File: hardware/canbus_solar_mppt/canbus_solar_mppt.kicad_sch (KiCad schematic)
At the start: 19 parts

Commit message: WIP: complete DC/DC engine
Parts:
- added F? (x2): MC011014, Fuse:Fuse_2920_7451Metric_Pad2.10x5.45mm_HandSolder, symbol Device:Polyfuse_Small
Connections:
- net DC-DC/SOLAR_PWR: now also F?.1; no longer D?.2 (A)
- net logic_canbus/CAN_PWR: now also F?.1; no longer D?.2 (A)
- new net: D?.2 (A), F?.2 (x2)
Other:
- moved on the sheet: D?

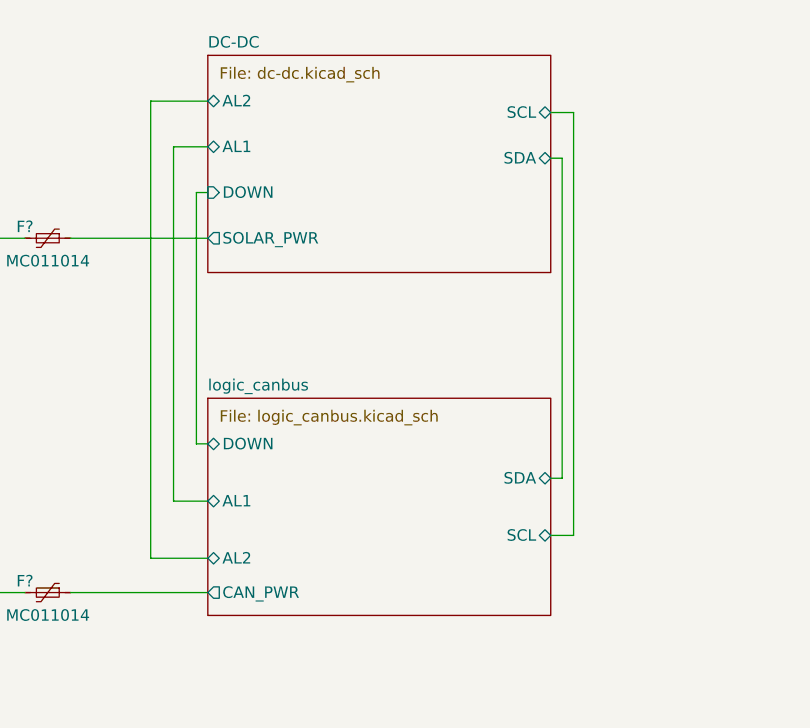
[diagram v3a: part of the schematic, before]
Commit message: Add more signals between pic18 and DC/DC
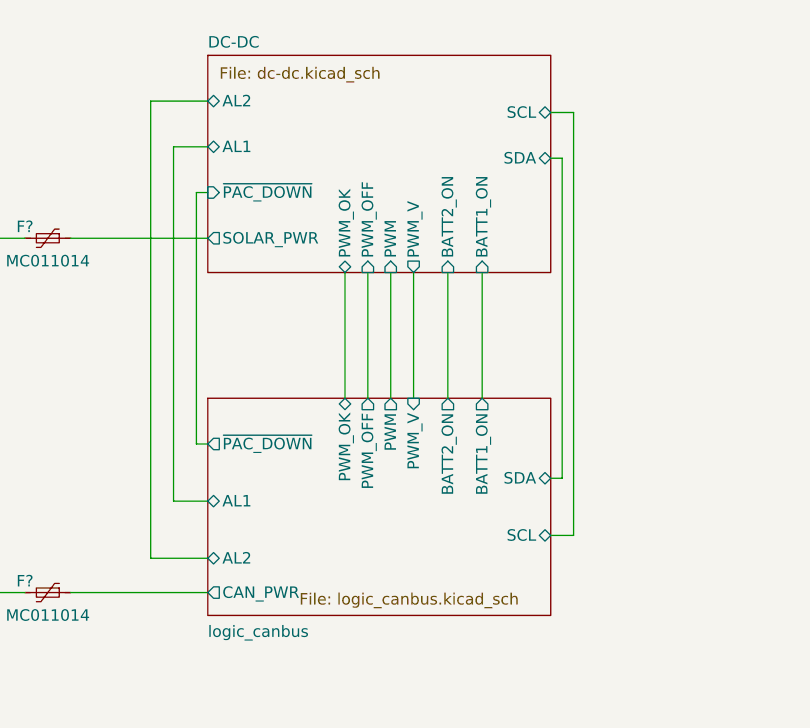
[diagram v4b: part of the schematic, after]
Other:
- sheet DC-DC ports: added BATT1_ON, BATT2_ON, PWM, PWM_OFF, PWM_OK, PWM_V, ~{PAC_DOWN}; removed DOWN
- sheet logic_canbus ports: added BATT1_ON, BATT2_ON, PWM, PWM_OFF, PWM_OK, PWM_V, ~{PAC_DOWN}; removed DOWN
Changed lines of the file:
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@@
+    (stroke (width 0) (type default) (color 0 0 0 0))
+  )
+  (wire (pts (xy 201.93 59.69) (xy 201.93 73.66))
     (stroke (width 0) (type default) (color 0 0 0 0))
   )
@@
     (stroke (width 0) (type default) (color 0 0 0 0))
   )
+  (wire (pts (xy 189.23 59.69) (xy 189.23 73.66))
+    (stroke (width 0) (type default) (color 0 0 0 0))
+  )
   (wire (pts (xy 63.5 93.98) (xy 53.34 93.98))
     (stroke (width 0) (type default) (color 0 0 0 0))
@@
     (stroke (width 0) (type default) (color 0 0 0 0))
   )
+  (wire (pts (xy 191.77 59.69) (xy 191.77 73.66))
+    (stroke (width 0) (type default) (color 0 0 0 0))
+  )
+  (wire (pts (xy 186.69 59.69) (xy 186.69 73.66))
+    (stroke (width 0) (type default) (color 0 0 0 0))
+  )
   (wire (pts (xy 119.38 86.36) (xy 119.38 87.63))
     (stroke (width 0) (type default) (color 0 0 0 0))
@@
     (stroke (width 0) (type default) (color 0 0 0 0))
   )
+  (wire (pts (xy 194.31 59.69) (xy 194.31 73.66))
+    (stroke (width 0) (type default) (color 0 0 0 0))
+  )
   (wire (pts (xy 165.1 40.64) (xy 165.1 91.44))
     (stroke (width 0) (type default) (color 0 0 0 0))
@@
   )
   (wire (pts (xy 53.34 67.31) (xy 57.15 67.31))
+    (stroke (width 0) (type default) (color 0 0 0 0))
+  )
+  (wire (pts (xy 198.12 59.69) (xy 198.12 73.66))
     (stroke (width 0) (type default) (color 0 0 0 0))
   )
@@
       (effects (font (size 1.27 1.27)) (justify left))
     )
-    (pin "DOWN" input (at 171.45 50.8 180)
-      (effects (font (size 1.27 1.27)) (justify left))
-    )
     (pin "SCL" bidirectional (at 209.55 41.91 0)
       (effects (font (size 1.27 1.27)) (justify right))
@@
     )
     (pin "SOLAR_PWR" output (at 171.45 55.88 180)
+      (effects (font (size 1.27 1.27)) (justify left))
+    )
+    (pin "BATT1_ON" input (at 201.93 59.69 270)
+      (effects (font (size 1.27 1.27)) (justify left))
+    )
+    (pin "PWM_V" output (at 194.31 59.69 270)
+      (effects (font (size 1.27 1.27)) (justify left))
+    )
+    (pin "BATT2_ON" input (at 198.12 59.69 270)
+      (effects (font (size 1.27 1.27)) (justify left))
+    )
+    (pin "PWM" input (at 191.77 59.69 270)
+      (effects (font (size 1.27 1.27)) (justify left))
+    )
+    (pin "PWM_OFF" input (at 189.23 59.69 270)
+      (effects (font (size 1.27 1.27)) (justify left))
+    )
+    (pin "PWM_OK" bidirectional (at 186.69 59.69 270)
+      (effects (font (size 1.27 1.27)) (justify left))
+    )
+    (pin "~{PAC_DOWN}" input (at 171.45 50.8 180)
       (effects (font (size 1.27 1.27)) (justify left))
     )
@@
     (stroke (width 0.1524) (type solid) (color 0 0 0 0))
     (fill (color 0 0 0 0.0000))
-    (property "Sheet name" "logic_canbus" (id 0) (at 171.45 72.9484 0)
+    (property "Sheet name" "logic_canbus" (id 0) (at 171.45 100.33 0)
       (effects (font (size 1.27 1.27)) (justify left bottom))
     )
-    (property "Sheet file" "logic_canbus.kicad_sch" (id 1) (at 172.72 74.93 0)
+    (property "Sheet file" "logic_canbus.kicad_sch" (id 1) (at 181.61 95.25 0)
       (effects (font (size 1.27 1.27)) (justify left top))
     )
@@
       (effects (font (size 1.27 1.27)) (justify right))
     )
-    (pin "DOWN" bidirectional (at 171.45 78.74 180)
+    (pin "~{PAC_DOWN}" output (at 171.45 78.74 180)
       (effects (font (size 1.27 1.27)) (justify left))
     )
@@
     (pin "CAN_PWR" output (at 171.45 95.25 180)
       (effects (font (size 1.27 1.27)) (justify left))
+    )
+    (pin "BATT1_ON" output (at 201.93 73.66 90)
+      (effects (font (size 1.27 1.27)) (justify right))
+    )
+    (pin "BATT2_ON" output (at 198.12 73.66 90)
+      (effects (font (size 1.27 1.27)) (justify right))
+    )
+    (pin "PWM_OFF" output (at 189.23 73.66 90)
+      (effects (font (size 1.27 1.27)) (justify right))
+    )
+    (pin "PWM_OK" bidirectional (at 186.69 73.66 90)
+      (effects (font (size 1.27 1.27)) (justify right))
+    )
+    (pin "PWM_V" input (at 194.31 73.66 90)
+      (effects (font (size 1.27 1.27)) (justify right))
+    )
+    (pin "PWM" output (at 191.77 73.66 90)
+      (effects (font (size 1.27 1.27)) (justify right))
     )
   )
@@
   )
   (symbol_instances
+    (path "/650b59c2-5f26-43cd-9e0c-72411aac3a49/02a51f57-3cf7-4e89-908d-048e0d55fd26"
+      (reference "#PWR?") (unit 1) (value "+5V") (footprint "")
+    )
     (path "/f749a8fe-5d5e-4748-ac37-3f3af8e2d0e8/046e9038-4a0e-4916-bc81-c5a27330b44e"
       (reference "#PWR?") (unit 1) (value "GND") (footprint "")
@@
       (reference "#PWR?") (unit 1) (value "GND") (footprint "")
     )
-    (path "/f749a8fe-5d5e-4748-ac37-3f3af8e2d0e8/befe8fb1-a994-45cc-8694-9d88f872ac5f"
-      (reference "#PWR?") (unit 1) (value "+5V") (footprint "")
-    )
     (path "/f749a8fe-5d5e-4748-ac37-3f3af8e2d0e8/bf27126d-2777-4e0c-8caa-229656dcb0fb"
       (reference "#PWR?") (unit 1) (value "+5V") (footprint "")
@@
     (path "/f749a8fe-5d5e-4748-ac37-3f3af8e2d0e8/c454ed80-5ad3-4205-b918-facb4559323c"
       (reference "#PWR?") (unit 1) (value "+5V") (footprint "")
-    )
-    (path "/f749a8fe-5d5e-4748-ac37-3f3af8e2d0e8/d0d5a83a-b1b9-4d26-908e-57f07485e447"
-      (reference "#PWR?") (unit 1) (value "GND") (footprint "")
     )
     (path "/650b59c2-5f26-43cd-9e0c-72411aac3a49/d743ffcd-5c13-44a3-b446-e3faf3dce348"
@@
       (reference "R?") (unit 1) (value "10K") (footprint "Resistor_THT:R_Axial_DIN0207_L6.3mm_D2.5mm_P7.62mm_Horizontal")
     )
-    (path "/f749a8fe-5d5e-4748-ac37-3f3af8e2d0e8/69c9f6b8-5c4a-495f-afae-470fc09b9bd9"
-      (reference "R?") (unit 1) (value "10K") (footprint "Resistor_SMD:R_1206_3216Metric_Pad1.30x1.75mm_HandSolder")
+    (path "/f749a8fe-5d5e-4748-ac37-3f3af8e2d0e8/723c4808-e36f-43cc-acdc-220d7731d5d3"
+      (reference "R?") (unit 1) (value "10K") (footprint "Resistor_THT:R_Axial_DIN0207_L6.3mm_D2.5mm_P7.62mm_Horizontal")
     )
     (path "/650b59c2-5f26-43cd-9e0c-72411aac3a49/758adae9-6fdc-4790-99a7-0cd4055f8e5d"
@@
       (reference "R?") (unit 1) (value "10K") (footprint "Resistor_SMD:R_1206_3216Metric_Pad1.30x1.75mm_HandSolder")
     )
+    (path "/650b59c2-5f26-43cd-9e0c-72411aac3a49/9d57c1ba-3976-407f-8594-55ec91182989"
+      (reference "R?") (unit 1) (value "56K") (footprint "Resistor_THT:R_Axial_DIN0207_L6.3mm_D2.5mm_P7.62mm_Horizontal")
+    )
+    (path "/f749a8fe-5d5e-4748-ac37-3f3af8e2d0e8/9e23f4d1-cd0b-4f93-b649-91a12ee681b7"
+      (reference "R?") (unit 1) (value "10K") (footprint "Resistor_THT:R_Axial_DIN0207_L6.3mm_D2.5mm_P7.62mm_Horizontal")
+    )
     (path "/f749a8fe-5d5e-4748-ac37-3f3af8e2d0e8/9fe30c66-4d14-474b-9ea7-7341b9aafecc"
       (reference "R?") (unit 1) (value "100") (footprint "Resistor_SMD:R_0805_2012Metric_Pad1.20x1.40mm_HandSolder")
@@
       (reference "R?") (unit 1) (value "100K") (footprint "Resistor_THT:R_Axial_DIN0207_L6.3mm_D2.5mm_P7.62mm_Horizontal")
     )
-    (path "/f749a8fe-5d5e-4748-ac37-3f3af8e2d0e8/c11df50c-99e5-4ff5-b4be-769ee4dfe14b"
-      (reference "TH?") (unit 1) (value "NTC10K") (footprint "TerminalBlock_TE-Connectivity:TerminalBlock_TE_282834-2_1x02_P2.54mm_Horizontal")
-    )
     (path "/f749a8fe-5d5e-4748-ac37-3f3af8e2d0e8/f24082c3-7636-411e-8431-8e24db80d342"

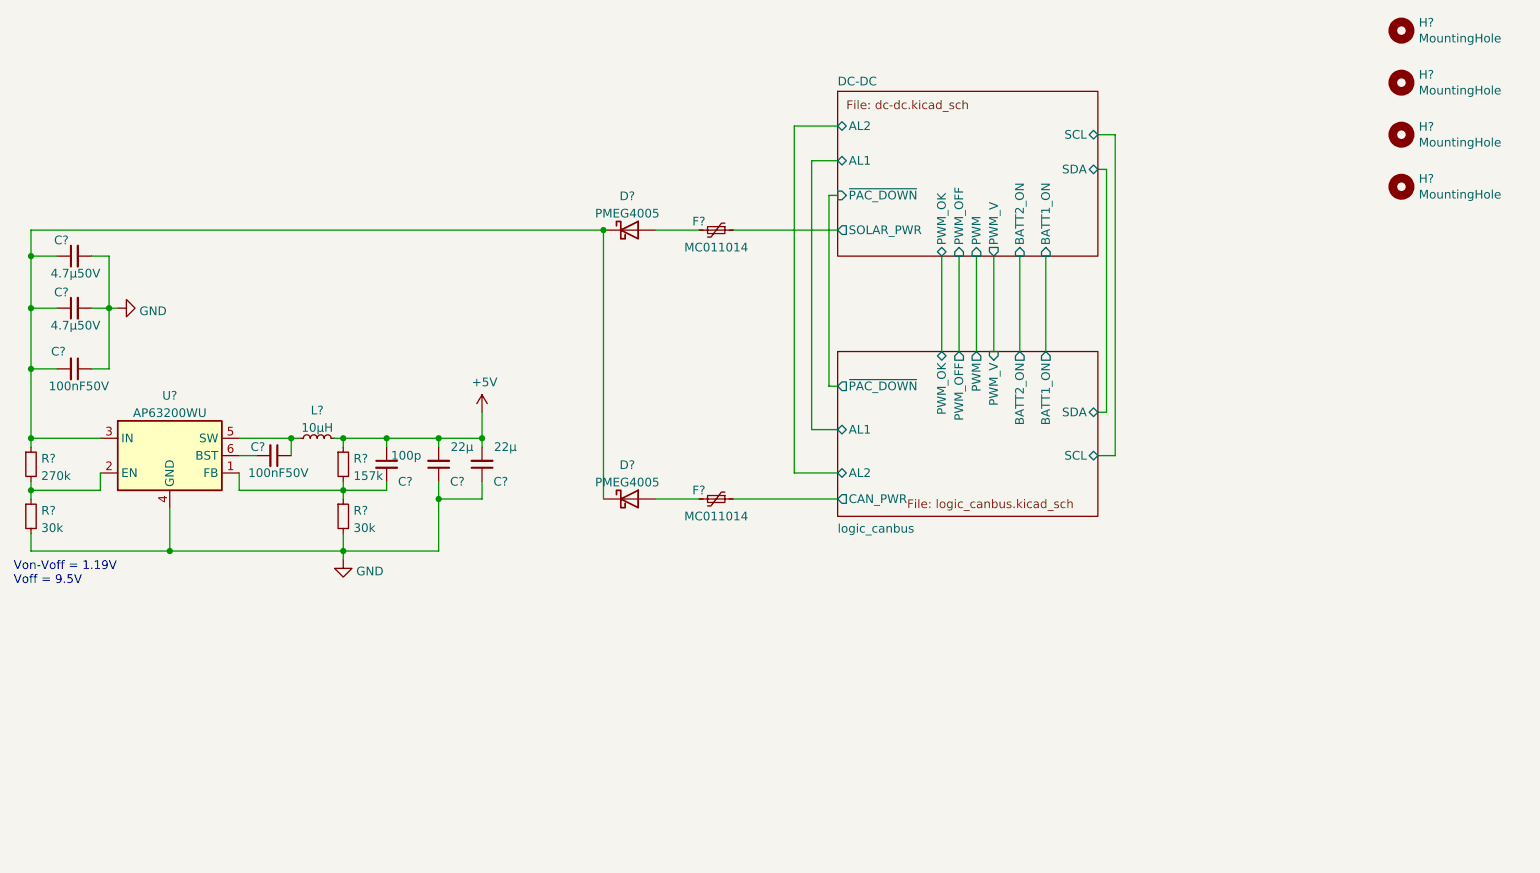
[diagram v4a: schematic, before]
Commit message: Add MCOB12864JX oled display. I2C-connected, not enough pic18 pins for SPI ...
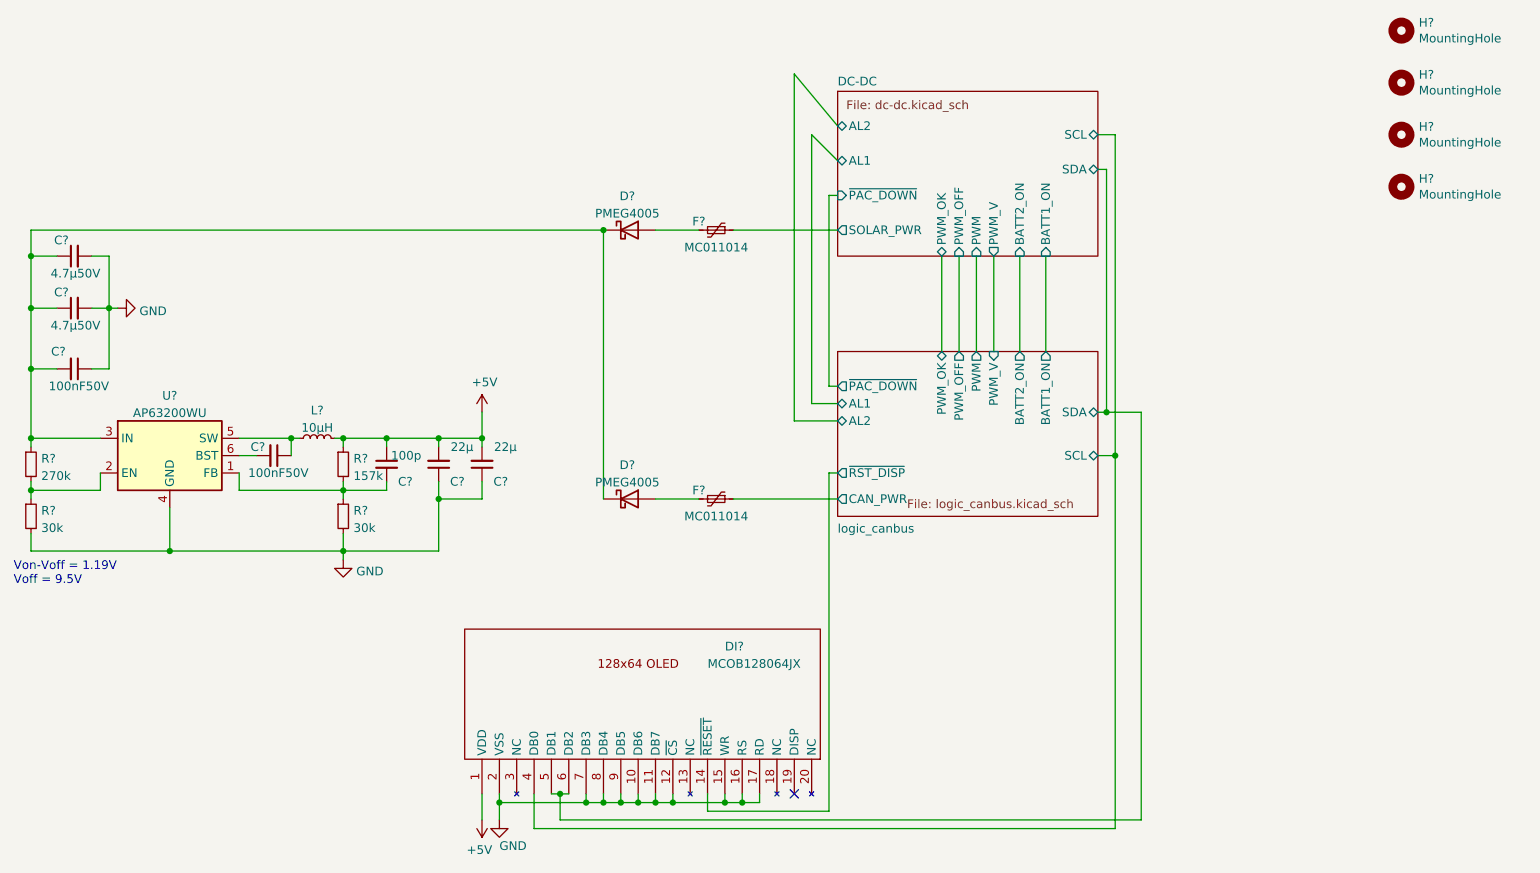
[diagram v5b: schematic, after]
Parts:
- added DI?: MCOB128064JX, symbol LCDdisplays:MCOB128064JX
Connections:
- net +5V: now also DI?.1 (VDD)
- net DC-DC/SCL: now also DI?.4 (DB0)
- net DC-DC/SDA: now also DI?.5 (DB1), DI?.6 (DB2)
- net GND: now also DI?.10 (DB6), DI?.11 (DB7), DI?.12 (~{CS}), DI?.15 (WR), DI?.16 (RS), DI?.17 (RD), DI?.2 (VSS), DI?.7 (DB3), DI?.8 (DB4), DI?.9 (DB5)
- new net logic_canbus/~{RST_DISP}: DI?.14 (~{RESET})
- no-connect marks 0 -> 1
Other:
- sheet logic_canbus ports: added ~{RST_DISP}; removed none

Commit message: Add 2 control buttons (could be more).
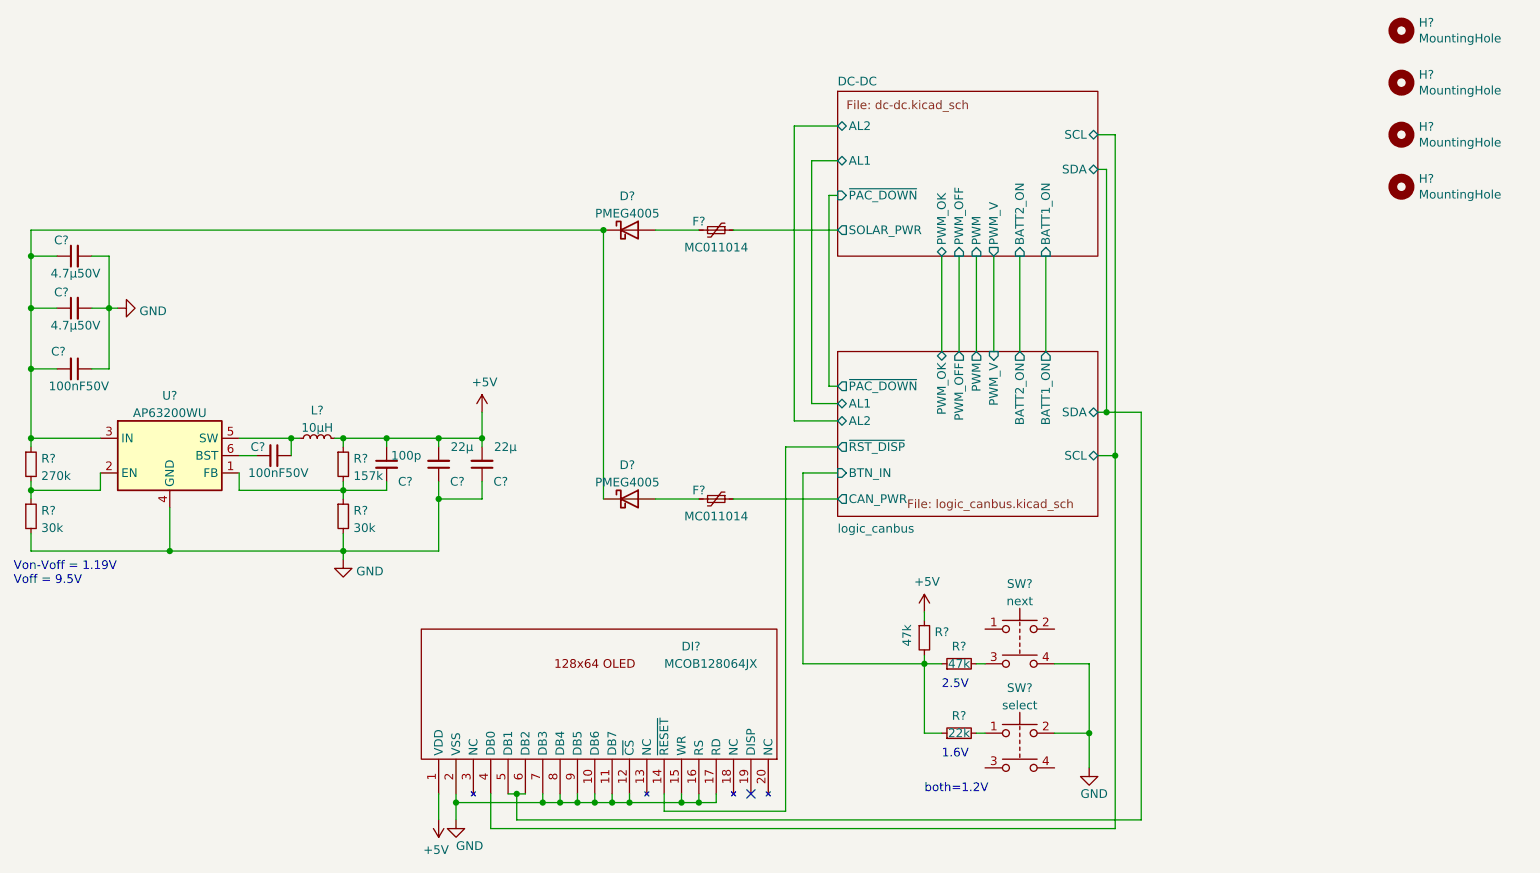
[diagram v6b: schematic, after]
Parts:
- added R? (x2): 47k, Resistor_SMD:R_0805_2012Metric_Pad1.20x1.40mm_HandSolder, symbol Device:R_Small
- added R?: 22k, Resistor_SMD:R_0805_2012Metric_Pad1.20x1.40mm_HandSolder, symbol Device:R_Small
- added SW?: select, Button_Switch_THT:Push_E-Switch_KS01Q01, symbol Switch:SW_Push_Dual
- added SW?: next, Button_Switch_THT:Push_E-Switch_KS01Q01, symbol Switch:SW_Push_Dual
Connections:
- net +5V: now also R?.1
- net GND: now also SW?.2, SW?.4
- new net: R?.2, SW?.3
- new net: R?.2, SW?.1
- new net logic_canbus/BTN_IN: R?.1, R?.1, R?.2
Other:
- sheet logic_canbus ports: added BTN_IN; removed none
- note added: "1.6V"
- note added: "2.5V"
- note added: "both=1.2V"
- moved on the sheet: DI?

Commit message: Add footprint for OLED display annotate schematic run and fix ERC
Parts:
- DI1: renamed from DI?; footprint (none) -> LCDdisplays.mod:MCOB128064JX; P/N (none) -> MCOB128064JX-YM
- gave numbers to parts that had none: 26
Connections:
- no-connect marks 1 -> 5
